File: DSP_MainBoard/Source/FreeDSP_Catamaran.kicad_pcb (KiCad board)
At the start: 2 copper layers, 100 x 100 mm, 253 parts, among them IC1 ADAU1701, IC2 24AA256, IC3 24AA256, J1 Conn_01x02, J10 Conn_01x02, J11 HeaderPin_01x03, J12 B3B-XH, J13 B3B-XH, J14 B3B-XH, J15 Molex 1718563002, J16 Conn_01x03, J2 Conn_RCA, J3 Conn_02x5_Odd_Even, J4 Conn_RCA, J5 Conn_RCA, J6 Conn_RCA, J7 Conn_01x06_Male, J8 Conn_RCA, J9 Conn_Power_2.1mm, P1 MIL-10P_Angle, Q1 2SC3326, Q10 AO3401A, Q11 AO3400A, Q12 AO3401A, Q13 AO3400A, Q2 AO3400A, Q3 2SC3326, Q5 2SC3326, Q6 AO3401A, Q7 2SC3326, Q8 KTA1040D-Y-RTF/P, Q9 AO3400A, SW1 2MS1T1B4M7QES, SW2 2MS1T1B4M7QES, U1 OPA1611, U2 SN74LV541APWR, U3 OPA1611, U4 OPA1611, U5 OPA1611, U6 AZ1117-ADJ, U7 AZ1117-ADJ, U8 OPA1611, U9 OPA1632DR, X2 3N12288G33YC

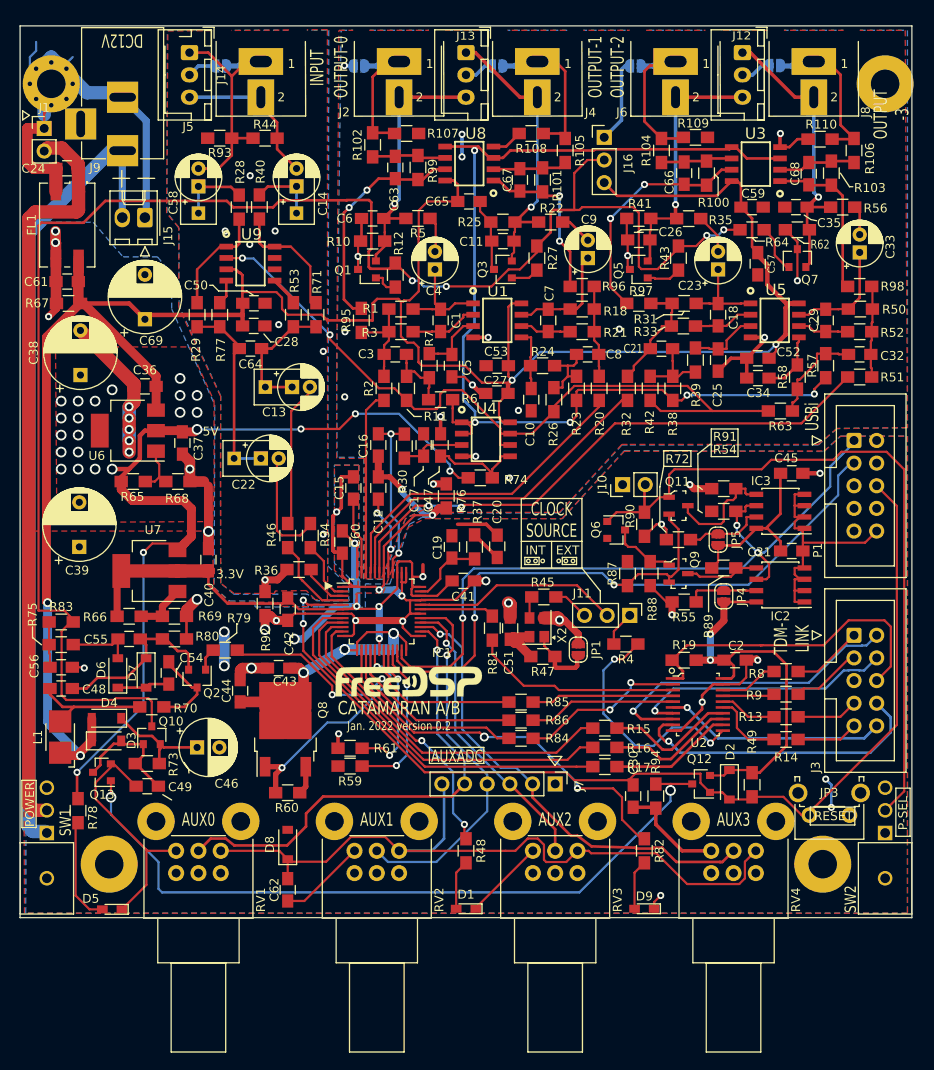
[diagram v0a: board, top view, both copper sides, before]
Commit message: FreeDSP Catamaran A/B version 0.21
Changed minor silkscreen layouts
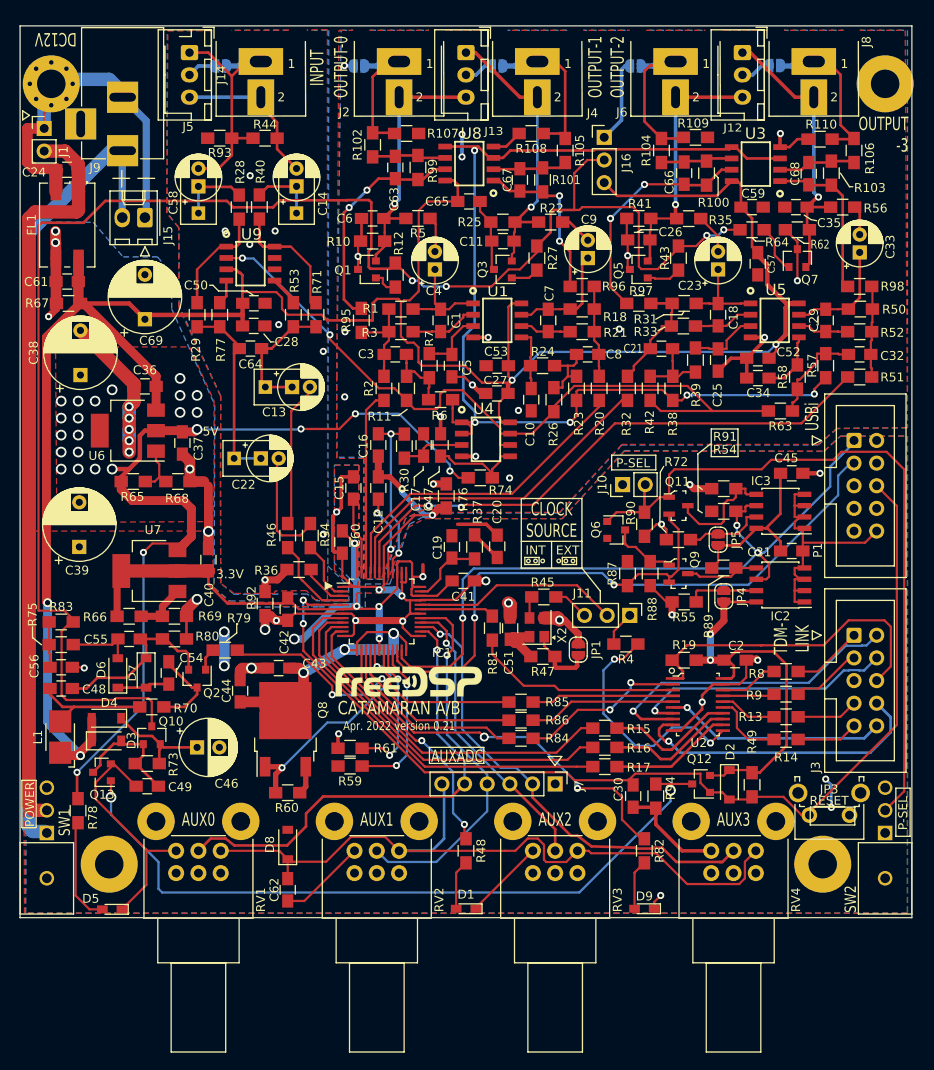
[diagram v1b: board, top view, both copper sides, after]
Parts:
- moved C24 0.16 mm to (55.3, 56.1)
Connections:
- P1 pad 2: (no net) -> Net-(P1-Pad2)
- P1 pad 4: (no net) -> Net-(P1-Pad4)
- P1 pad 5: (no net) -> Net-(P1-Pad5)
- P1 pad 7: (no net) -> Net-(P1-Pad7)
- P1 pad 8: (no net) -> Net-(P1-Pad8)
- P1 pad 9: (no net) -> Net-(P1-Pad9)
- SW1 pad 3: (no net) -> Net-(SW1-Pad3)
- SW2 pad 3: (no net) -> Net-(SW2-Pad3)
- U9 pad 7: (no net) -> Net-(U9-Pad7)
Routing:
- net Earth: track 57.6 -> 52.6 mm
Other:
- board text added: "Apr. 2022 version 0.21"
- board text removed: "Jan. 2022 version 0.2"

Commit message: Version 1.0 Release Ki-CAD Data Files
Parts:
- added C70: 100n, Capacitors_SMD:C_0805_HandSoldering, F.Cu at (68.9, 95.1)
- J7: value Conn_01x06_Male -> Conn_01x07_Male; footprint Connector_PinHeader_2.54mm:PinHeader_1x06_P2.54mm_Vertical -> Connector_PinHeader_2.54mm:PinHeader_1x07_P2.54mm_Vertical
- R34, R36, R46: value 10k -> 18k
- R87, R89, R91: value 4.7k -> 1k
- U4: value OPA1611 -> OPA1652
- moved C39 17.5 mm to (74.1, 97.4)
- moved C22 2.14 mm to (77.0, 86.4)
- moved C69 0.22 mm to (64.1, 72.7)
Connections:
- R15 pad 2: /MP1 -> /MP0
- R48 pad 1: /MP0 -> /MP1
- U7 pad 3: +5V -> +12V
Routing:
- net +12V: track 260.2 -> 281.5 mm
- net +5V: track 100.0 -> 90.3 mm, vias 25 -> 33
- net /MP1: track 40.4 -> 32.3 mm, vias 0 -> 2
- net /MP0: track 30.8 -> 38.3 mm, vias 2 -> 0
- net 3V3: track 175.4 -> 181.6 mm, vias 13 -> 41
- net Net-(C22-Pad1): track 21.5 -> 19.3 mm
- net /POS: track 12.8 -> 14.9 mm
- net /BRD_~RESET: track 118.8 -> 120.4 mm
- net GND: track 264.2 -> 263.9 mm, vias 32 -> 27
- added copper zone on B.Cu, net +5V
- added copper zone on B.Cu, net 3V3
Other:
- board text added: "+1.5V"
- board text added: "Apr. 2022 version 1.0"
- board text added: "MP1"
- board text removed: "Apr. 2022 version 0.21"
- board text removed: "MP0"

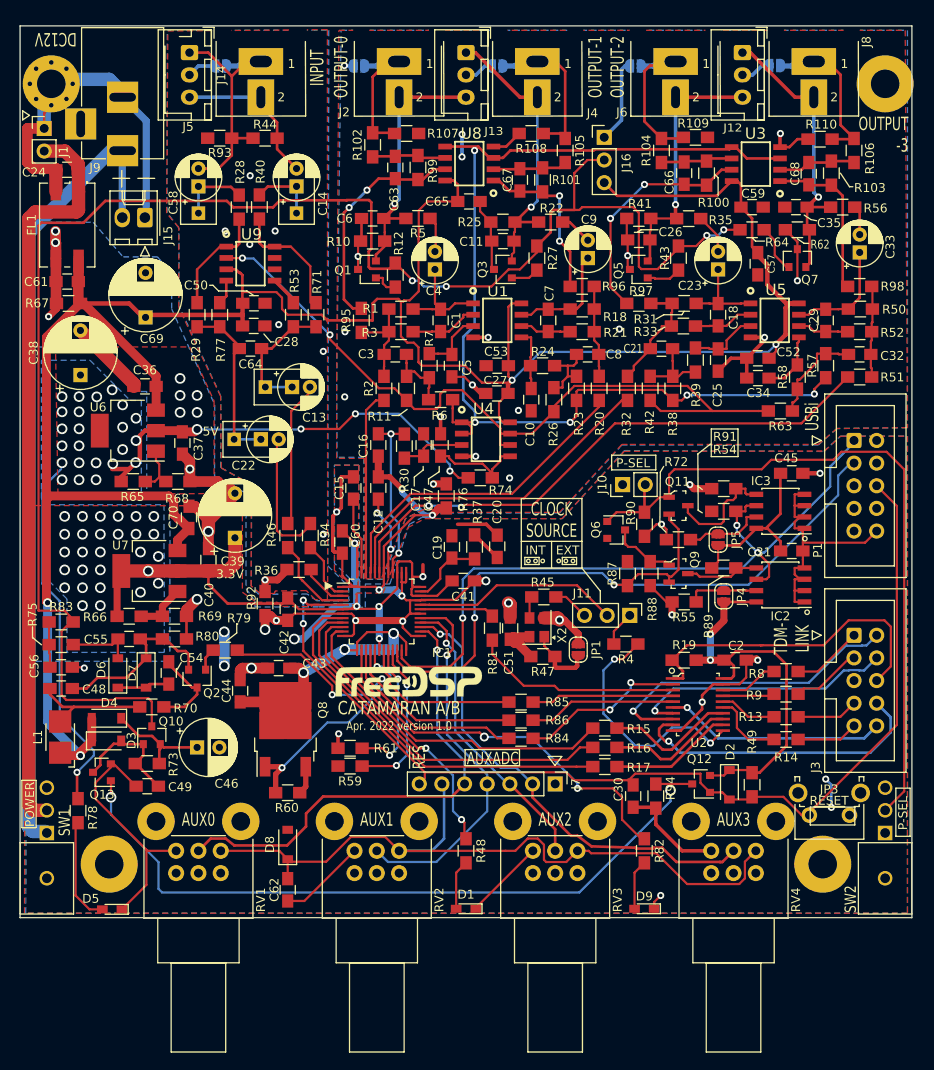
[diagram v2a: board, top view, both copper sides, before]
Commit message: 1v2 add auto-reboot feature on PGM-SW transnsition
The reset switch was removed due to the automatic DSP reboot feature on the transition of the A/B program change.
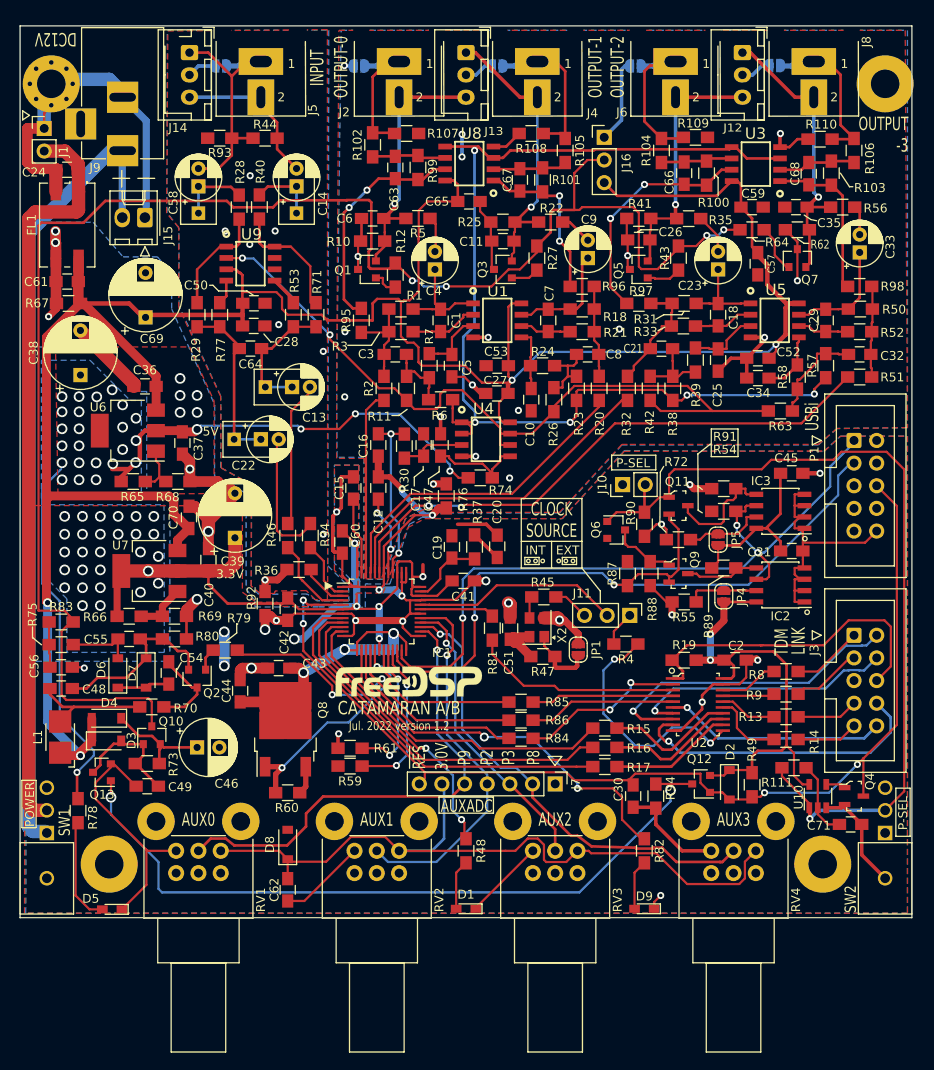
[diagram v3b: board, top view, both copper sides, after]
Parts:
- removed JP3: TACT_ANGLE_PUSH, Button_Switch_THT:SW_Tactile_SPST_Angled_PTS645Vx83-2LFS
- added C71: 100n, Capacitors_SMD:C_0805_HandSoldering, F.Cu at (143.1, 129.5)
- added Q4: AO3400A, digikey-footprints:SOT-23-3, F.Cu at (143.5, 126.4)
- added R111: 1MEG, Resistors_SMD:R_0805_HandSoldering, F.Cu at (136.8, 123.2)
- added U10: SN74LVC1G86DBVR, Package_TO_SOT_SMD:TSOT-23-5, F.Cu at (139.4, 126.4)
- R29: value 10k -> 20k
- R34, R36, R46: value 18k -> 15k
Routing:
- net Net-(J10-Pad2): track 81.4 -> 97.4 mm, vias 0 -> 1
- net GND: track 263.9 -> 276.3 mm
- net Net-(C71-Pad2): track 0.00 -> 8.66 mm
- net 3V3: track 181.6 -> 185.1 mm, vias 41 -> 39
- net /BRD_~RESET: track 120.4 -> 122.7 mm, vias 2 -> 4
- net /PCHG: track 0.00 -> 2.21 mm
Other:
- board text added: "3.0V"
- board text added: "Jul. 2022 version 1.2"
- board text added: "LINK"
- board text added: "P2"
- board text added: "P3"
- board text added: "P8"
- board text added: "P9"
- board text added: "TDM"
- board text removed: "Apr. 2022 version 1.0"
- board text removed: "RESET"
- board text removed: "TDM- LINK"
